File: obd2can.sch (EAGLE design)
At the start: 18 parts, among them Q1 16MHz, SW3 6X3.5_TACT, U2 SN65HVD235DR, U3 STM32F030XTSSOP20, U4 MCP1700, X1 RJ45_RIGHT_ANGLEMOLEX_95001-2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

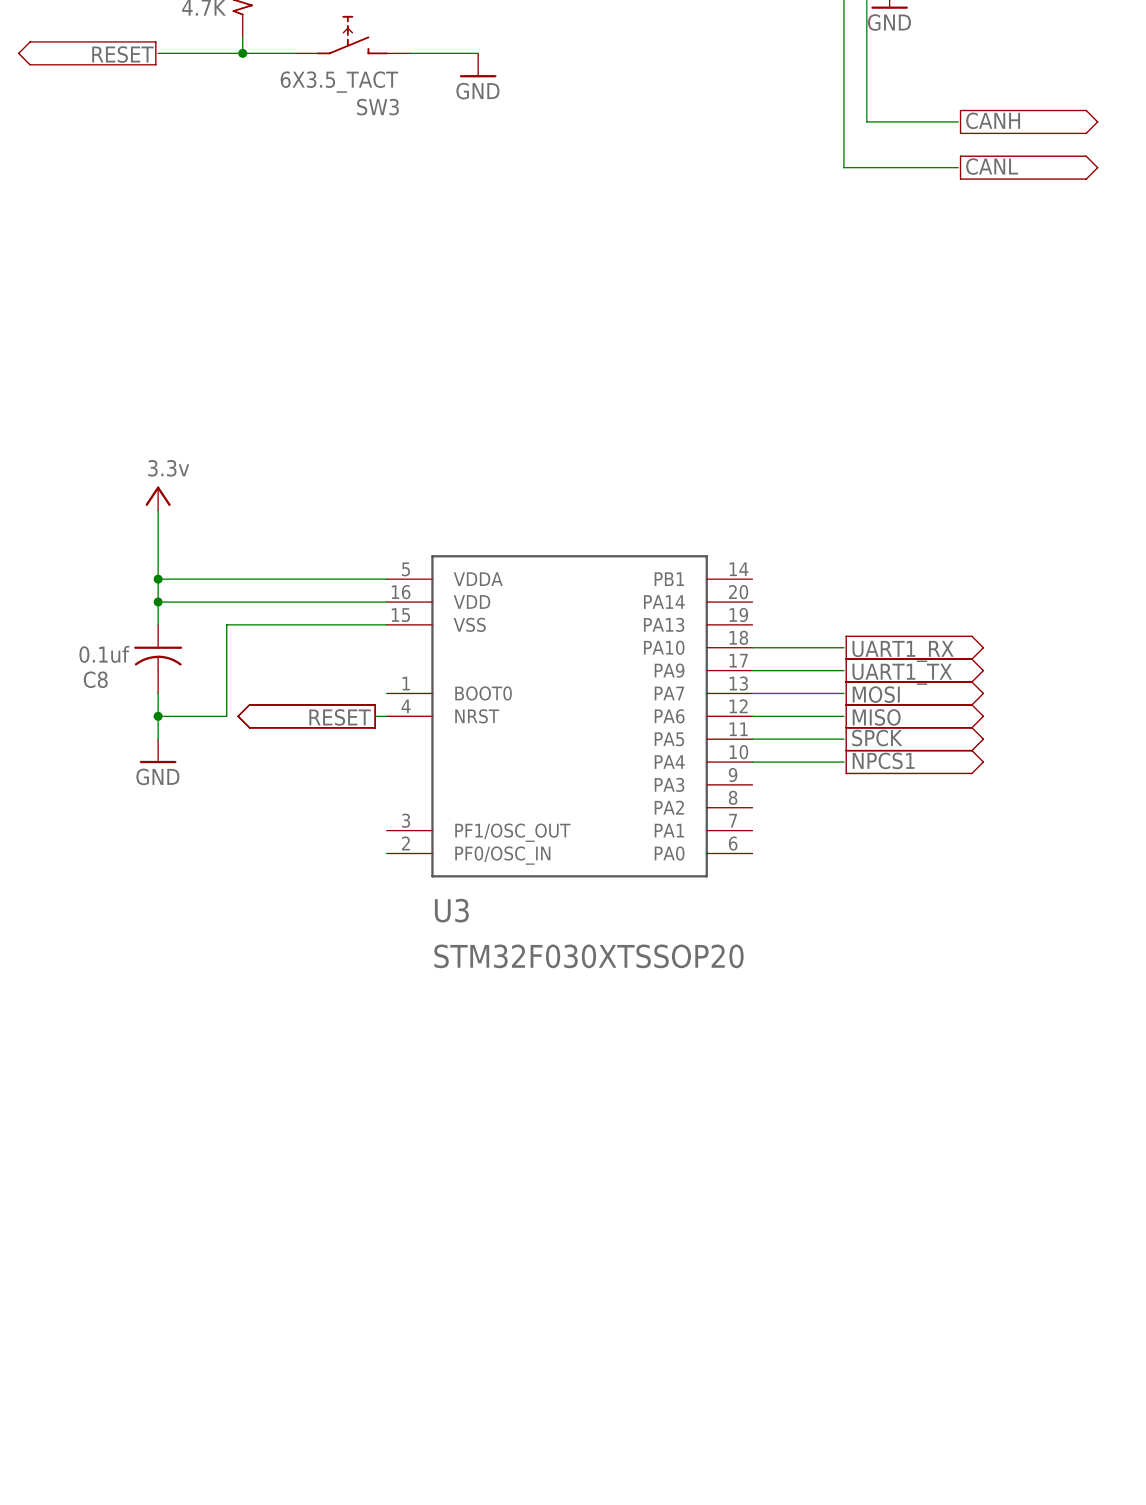
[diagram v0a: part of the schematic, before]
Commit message: added swdebug and boot button
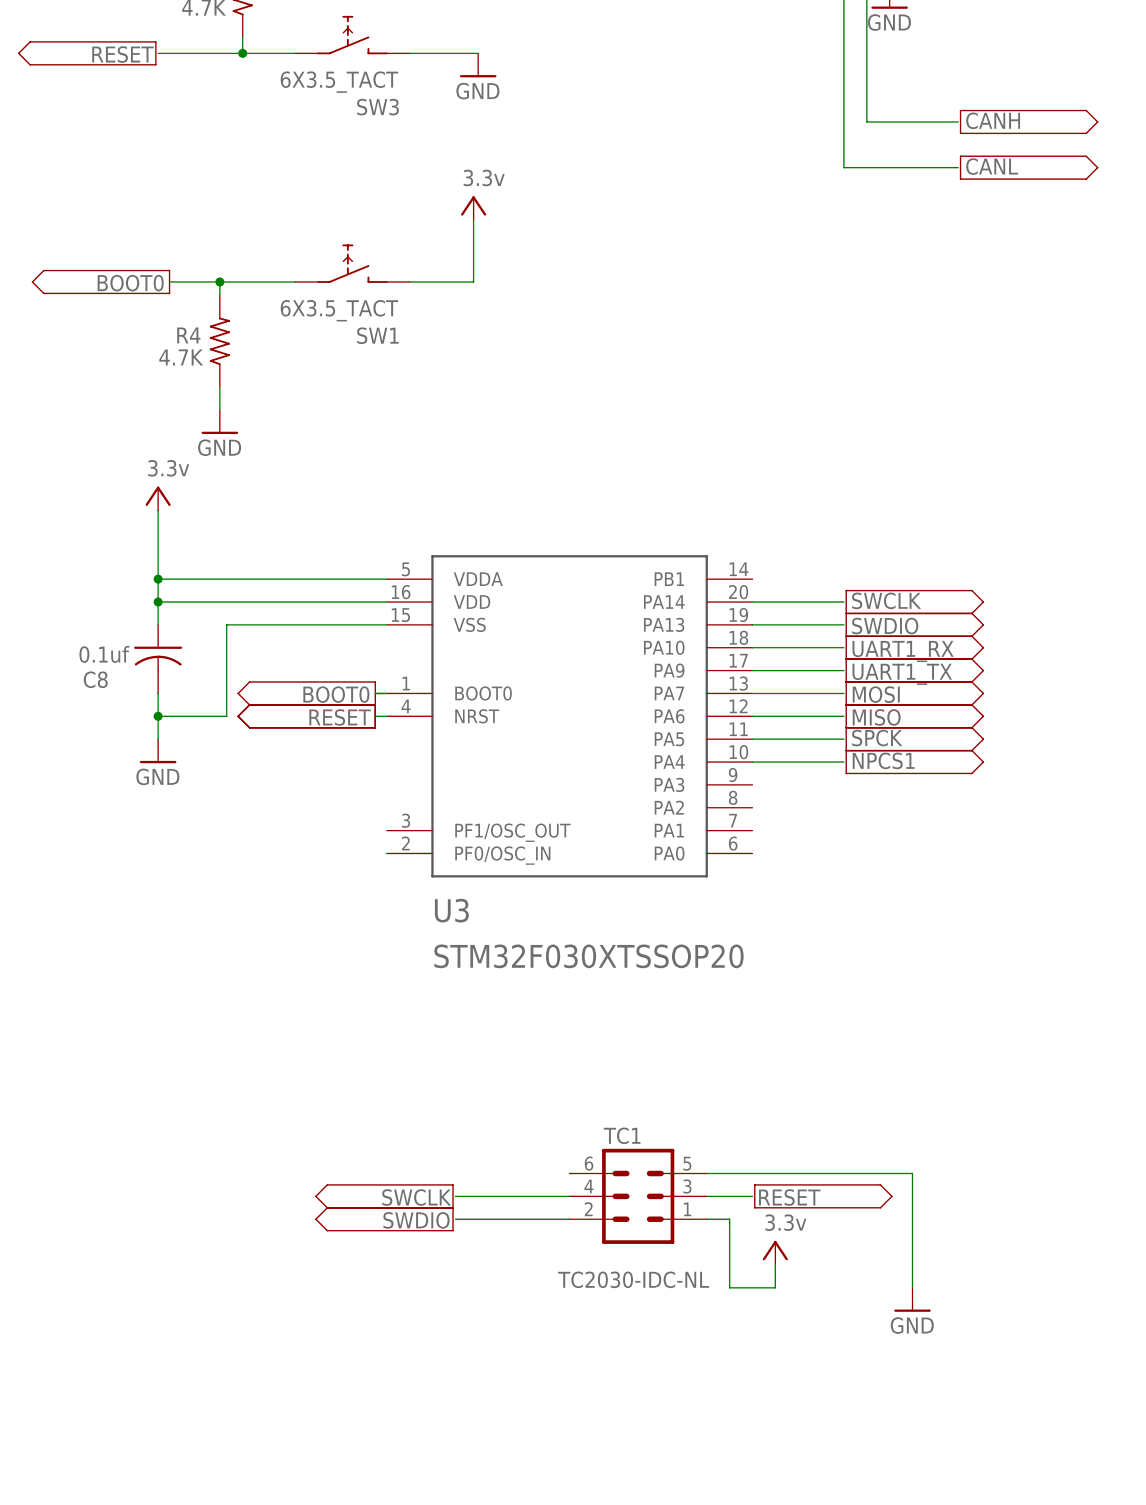
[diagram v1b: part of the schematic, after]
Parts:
- added R4: 4.7K, rcl:R-US_R0603
- added SW1: 6X3.5_TACT, tactile_switch:6X3.5_TACT
- added TC1: TC2030-IDC-NL, TagConnect:TC2030-IDC-NL
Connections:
- new net BOOT0: R4.2, SW1.1, U3.BOOT0
- new net SWCLK: TC1.4, U3.PA14
- new net SWDIO: TC1.2, U3.PA13
- net GND: now also R4.1, TC1.5
- net RESET: now also TC1.3
- net V+: now also SW1.2, TC1.1
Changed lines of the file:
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@@
 <part name="R3" library="rcl" deviceset="R-US_" device="R0603" value="4.7K"/>
 <part name="P+8" library="supply2" deviceset="V+" device="" value="3.3v"/>
+<part name="TC1" library="TagConnect" deviceset="TC2030-IDC" device="-NL"/>
+<part name="GND6" library="supply1" deviceset="GND" device=""/>
+<part name="P+9" library="supply2" deviceset="V+" device="" value="3.3v"/>
+<part name="AD14" library="supply2" deviceset="V--&gt;" device="" value=""/>
+<part name="AD15" library="supply2" deviceset="V--&gt;" device="" value=""/>
+<part name="AD16" library="supply2" deviceset="V--&gt;" device="" value=""/>
+<part name="AD17" library="supply2" deviceset="V--&gt;" device="" value=""/>
+<part name="AD18" library="supply2" deviceset="V--&gt;" device="" value=""/>
+<part name="AD19" library="supply2" deviceset="V--&gt;" device="" value=""/>
+<part name="SW1" library="tactile_switch" deviceset="6X3.5_TACT" device=""/>
+<part name="R4" library="rcl" deviceset="R-US_" device="R0603" value="4.7K"/>
+<part name="GND9" library="supply1" deviceset="GND" device=""/>
+<part name="P+10" library="supply2" deviceset="V+" device="" value="3.3v"/>
+<part name="AD20" library="supply2" deviceset="V--&gt;" device="" value=""/>
 </parts>
 <sheets>
@@
 </instance>
 <instance part="P+8" gate="1" x="-71.882" y="38.862"/>
+<instance part="TC1" gate="A" x="-27.94" y="-106.68" smashed="yes">
+<attribute name="VALUE" x="-36.83" y="-116.84" size="1.778" layer="96"/>
+<attribute name="NAME" x="-31.75" y="-100.838" size="1.778" layer="95"/>
+</instance>
+<instance part="GND6" gate="1" x="2.54" y="-119.38"/>
+<instance part="P+9" gate="1" x="-12.7" y="-111.76"/>
+<instance part="AD14" gate="G$1" x="-48.514" y="-109.22" smashed="yes" rot="R180">
+<attribute name="VALUE" x="-49.784" y="-108.458" size="1.778" layer="96" rot="R180"/>
+</instance>
+<instance part="AD15" gate="G$1" x="-48.514" y="-106.68" smashed="yes" rot="R180">
+<attribute name="VALUE" x="-49.784" y="-105.918" size="1.778" layer="96" rot="R180"/>
+</instance>
+<instance part="AD16" gate="G$1" x="-14.986" y="-106.68" smashed="yes">
+<attribute name="VALUE" x="-13.716" y="-107.442" size="1.778" layer="96"/>
+</instance>
+<instance part="AD17" gate="G$1" x="-4.826" y="-43.18" smashed="yes">
+<attribute name="VALUE" x="-3.556" y="-43.942" size="1.778" layer="96"/>
+</instance>
+<instance part="AD18" gate="G$1" x="-4.826" y="-40.64" smashed="yes">
+<attribute name="VALUE" x="-3.556" y="-41.402" size="1.778" layer="96"/>
+</instance>
+<instance part="AD19" gate="G$1" x="-57.15" y="-50.8" smashed="yes" rot="R180">
+<attribute name="VALUE" x="-58.42" y="-50.038" size="1.778" layer="96" rot="R180"/>
+</instance>
+<instance part="SW1" gate="G$1" x="-60.96" y="-5.08" smashed="yes">
+<attribute name="NAME" x="-54.356" y="-10.16" size="1.778" layer="95" rot="R180"/>
+<attribute name="VALUE" x="-54.61" y="-7.112" size="1.778" layer="96" rot="R180"/>
+</instance>
+<instance part="R4" gate="G$1" x="-74.422" y="-11.684" smashed="yes" rot="R90">
+<attribute name="NAME" x="-76.454" y="-10.1346" size="1.778" layer="95" rot="R180"/>
+<attribute name="VALUE" x="-76.327" y="-12.573" size="1.778" layer="96" rot="R180"/>
+</instance>
+<instance part="GND9" gate="1" x="-74.422" y="-21.844"/>
+<instance part="P+10" gate="1" x="-46.228" y="4.318"/>
+<instance part="AD20" gate="G$1" x="-80.01" y="-5.08" smashed="yes" rot="R180">
+<attribute name="VALUE" x="-81.28" y="-4.318" size="1.778" layer="96" rot="R180"/>
+</instance>
 </instances>
 <busses>
@@
 <pinref part="SW3" gate="G$1" pin="2"/>
 <pinref part="GND46" gate="1" pin="GND"/>
+</segment>
+<segment>
+<pinref part="GND6" gate="1" pin="GND"/>
+<wire x1="2.54" y1="-104.14" x2="2.54" y2="-116.84" width="0.1524" layer="91"/>
+<pinref part="TC1" gate="A" pin="5"/>
+<wire x1="2.54" y1="-104.14" x2="-20.32" y2="-104.14" width="0.1524" layer="91"/>
+</segment>
+<segment>
+<pinref part="R4" gate="G$1" pin="1"/>
+<pinref part="GND9" gate="1" pin="GND"/>
+<wire x1="-74.422" y1="-19.304" x2="-74.422" y2="-16.764" width="0.1524" layer="91"/>
 </segment>
 </net>
@@
 <wire x1="-71.882" y1="36.322" x2="-71.882" y2="32.258" width="0.1524" layer="91"/>
 </segment>
+<segment>
+<pinref part="TC1" gate="A" pin="1"/>
+<wire x1="-20.32" y1="-109.22" x2="-17.78" y2="-109.22" width="0.1524" layer="91"/>
+<wire x1="-17.78" y1="-109.22" x2="-17.78" y2="-116.84" width="0.1524" layer="91"/>
+<pinref part="P+9" gate="1" pin="V+"/>
+<wire x1="-17.78" y1="-116.84" x2="-12.7" y2="-116.84" width="0.1524" layer="91"/>
+<wire x1="-12.7" y1="-116.84" x2="-12.7" y2="-114.3" width="0.1524" layer="91"/>
+</segment>
+<segment>
+<pinref part="P+10" gate="1" pin="V+"/>
+<pinref part="SW1" gate="G$1" pin="2"/>
+<wire x1="-46.228" y1="1.778" x2="-46.228" y2="-5.08" width="0.1524" layer="91"/>
+<wire x1="-46.228" y1="-5.08" x2="-53.34" y2="-5.08" width="0.1524" layer="91"/>
+</segment>
 </net>
 <net name="UART1_TX" class="0">
@@
 <label x="-57.658" y="-52.578" size="1.778" layer="95" rot="R180"/>
 </segment>
+<segment>
+<pinref part="TC1" gate="A" pin="3"/>
+<wire x1="-20.32" y1="-106.68" x2="-15.24" y2="-106.68" width="0.1524" layer="91"/>
+<label x="-14.732" y="-107.696" size="1.778" layer="95"/>
+</segment>
 </net>
+<net name="SWDIO" class="0">
+<segment>
+<pinref part="TC1" gate="A" pin="2"/>
+<wire x1="-35.56" y1="-109.22" x2="-48.26" y2="-109.22" width="0.1524" layer="91"/>
+<label x="-48.768" y="-108.458" size="1.778" layer="95" rot="R180"/>
+</segment>
+<segment>
+<pinref part="U3" gate="G$1" pin="PA13"/>
+<wire x1="-15.24" y1="-43.18" x2="-5.08" y2="-43.18" width="0.1524" layer="91"/>
+<label x="-4.318" y="-44.196" size="1.778" layer="95"/>
+</segment>
+</net>
+<net name="SWCLK" class="0">
+<segment>
+<pinref part="TC1" gate="A" pin="4"/>
+<wire x1="-35.56" y1="-106.68" x2="-48.26" y2="-106.68" width="0.1524" layer="91"/>
+<label x="-48.768" y="-105.918" size="1.778" layer="95" rot="R180"/>
+</segment>
+<segment>
+<pinref part="U3" gate="G$1" pin="PA14"/>
+<wire x1="-15.24" y1="-40.64" x2="-5.08" y2="-40.64" width="0.1524" layer="91"/>
+<label x="-4.318" y="-41.402" size="1.778" layer="95"/>
+</segment>
+</net>
+<net name="BOOT0" class="0">
+<segment>
+<pinref part="U3" gate="G$1" pin="BOOT0"/>
+<wire x1="-55.88" y1="-50.8" x2="-57.15" y2="-50.8" width="0.1524" layer="91"/>
+<wire x1="-55.88" y1="-50.8" x2="-57.15" y2="-50.8" width="0.1524" layer="91"/>
+<label x="-57.658" y="-50.038" size="1.778" layer="95" rot="R180"/>
+</segment>
+<segment>
+<pinref part="SW1" gate="G$1" pin="1"/>
+<wire x1="-66.04" y1="-5.08" x2="-74.422" y2="-5.08" width="0.1524" layer="91"/>
+<pinref part="R4" gate="G$1" pin="2"/>
+<wire x1="-74.422" y1="-5.08" x2="-80.01" y2="-5.08" width="0.1524" layer="91"/>
+<wire x1="-74.422" y1="-6.604" x2="-74.422" y2="-5.08" width="0.1524" layer="91"/>
+<junction x="-74.422" y="-5.08"/>
+<label x="-80.518" y="-4.318" size="1.778" layer="95" rot="R180"/>
+</segment>
+</net>

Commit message: minor label updates
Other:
- note added: "Copyright 2014 Autosport Labs"
- note added: "OBD to CAN bus bridge"
- note added: "OBD2CAN"
- note removed: "CAN bus expansion for RaceCapture/Pro"
- note removed: "CANx"
- note removed: "Copyright 2012-2013 Autosport Labs"
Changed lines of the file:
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@@
 <setting verticaltext="up"/>
 </settings>
-<grid distance="0.01" unitdist="inch" unit="inch" style="lines" multiple="1" display="no" altdistance="0.01" altunitdist="inch" altunit="inch"/>
+<grid distance="0.1" unitdist="inch" unit="inch" style="lines" multiple="1" display="no" altdistance="0.01" altunitdist="inch" altunit="inch"/>
 <layers>
 <layer number="1" name="Top" color="4" fill="1" visible="no" active="no"/>
@@
 <sheet>
 <plain>
-<text x="353.06" y="175.26" size="6.4516" layer="97" rot="R180">Copyright 2012-2013 Autosport Labs</text>
-<text x="353.06" y="195.58" size="6.4516" layer="97" rot="R180">CANx</text>
+<text x="353.06" y="175.26" size="6.4516" layer="97" rot="R180">Copyright 2014 Autosport Labs</text>
+<text x="353.06" y="195.58" size="6.4516" layer="97" rot="R180">OBD2CAN</text>
 <text x="265.43" y="206.883" size="6.4516" layer="97" font="vector">autosportlabs.net</text>
 <text x="359.918" y="-179.832" size="5.08" layer="97">A</text>
-<text x="353.06" y="185.42" size="6.4516" layer="97" rot="R180">CAN bus expansion for RaceCapture/Pro</text>
+<text x="353.06" y="185.42" size="6.4516" layer="97" rot="R180">OBD to CAN bus bridge</text>
 <rectangle x1="284.6705" y1="215.9635" x2="355.5365" y2="216.0905" layer="97"/>
 <rectangle x1="284.6705" y1="216.0905" x2="355.5365" y2="216.2175" layer="97"/>

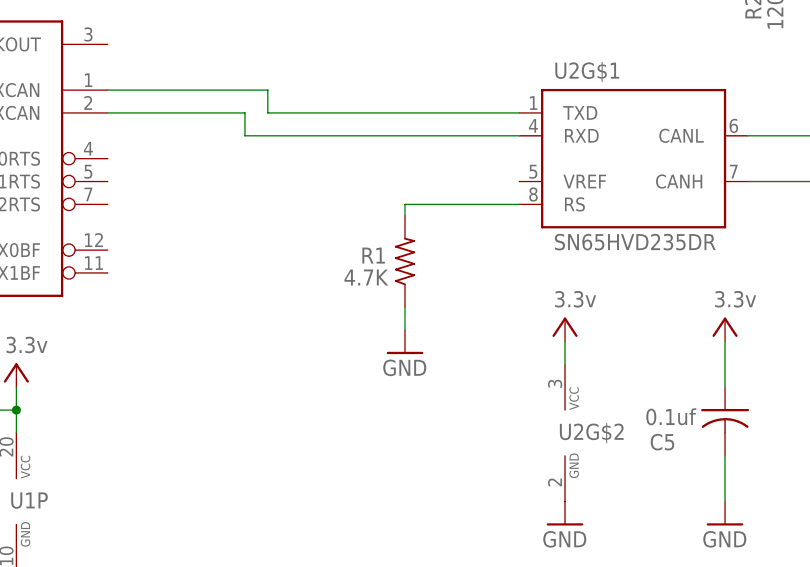
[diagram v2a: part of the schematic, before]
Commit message: grounded vref pin on can transceiver
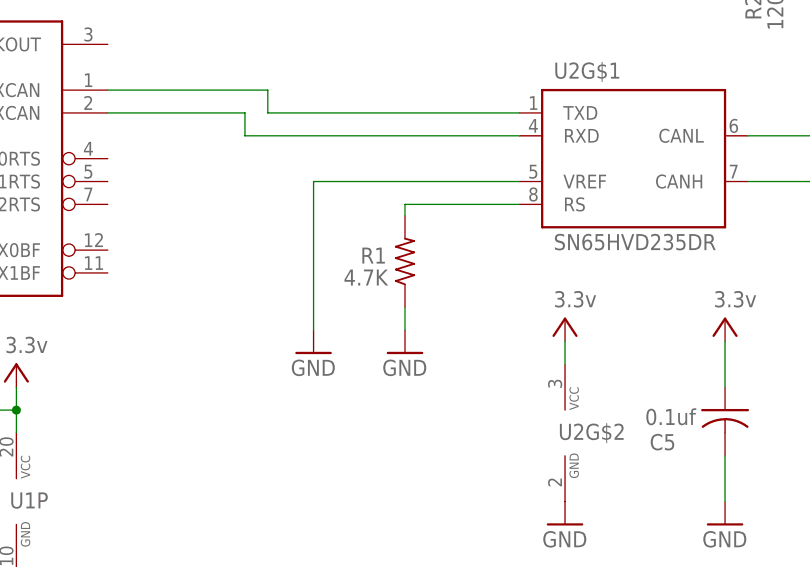
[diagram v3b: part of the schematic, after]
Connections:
- net GND: now also U2G$1.VREF
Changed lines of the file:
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@@
 <setting verticaltext="up"/>
 </settings>
-<grid distance="0.1" unitdist="inch" unit="inch" style="lines" multiple="1" display="no" altdistance="0.01" altunitdist="inch" altunit="inch"/>
+<grid distance="0.01" unitdist="inch" unit="inch" style="lines" multiple="1" display="no" altdistance="0.01" altunitdist="inch" altunit="inch"/>
 <layers>
 <layer number="1" name="Top" color="4" fill="1" visible="no" active="no"/>
@@
 <part name="P+10" library="supply2" deviceset="V+" device="" value="3.3v"/>
 <part name="AD20" library="supply2" deviceset="V--&gt;" device="" value=""/>
+<part name="GND11" library="supply1" deviceset="GND" device=""/>
 </parts>
 <sheets>
@@
 <attribute name="VALUE" x="-81.28" y="-4.318" size="1.778" layer="96" rot="R180"/>
 </instance>
+<instance part="GND11" gate="1" x="142.24" y="13.97"/>
 </instances>
 <busses>
@@
 <wire x1="-74.422" y1="-19.304" x2="-74.422" y2="-16.764" width="0.1524" layer="91"/>
 </segment>
+<segment>
+<pinref part="U2" gate="G$1" pin="VREF"/>
+<wire x1="165.1" y1="33.02" x2="142.24" y2="33.02" width="0.1524" layer="91"/>
+<wire x1="142.24" y1="33.02" x2="142.24" y2="16.51" width="0.1524" layer="91"/>
+<pinref part="GND11" gate="1" pin="GND"/>
+</segment>
 </net>

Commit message: OBD2CAN WIP
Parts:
- removed C4: 0.1uF, rcl:C-USC0603K
- removed C6: 10uF, rcl:CPOL-USSMCA
- removed C8: 0.1uf, rcl:C-USC0603K
- removed SW1, SW3: 6X3.5_TACT, tactile_switch:6X3.5_TACT
- removed TC1: TC2030-IDC-NL, TagConnect:TC2030-IDC-NL
- removed U4: MCP1700, mcp1700:MCP1700
- added C10: 1uf, rcl:C-USC0603K
- added C11: 0.01uf, rcl:C-USC0603K
- added C12, C15: 4.7uf, rcl:C-USC0603K
- added C14, C9: 0.1uf, rcl:C-USC0603K
- added C25, C28: 22uF, rcl:C-USC1206
- added C27: 10nF, rcl:C-USC0603
- added D1: SCHOTTKY, smt_diodes:SCHOTTKY
- added D2: 400V 1A, smt_diodes:DIODE1
- added D5: (no value), diode:SCHOTTKY-DIODESMC
- added L1: 4.7uH, rcl:L-EUL2012C
- added L2: (no value), wuerth-elektronik:WE-CBF_1812
- added R5: 4.7K, rcl:R-US_R0603
- added SW2: 6X3.5_TACT, tactile_switch:6X3.5_TACT
- added TC2: TC2030-IDC-NL, TagConnect:TC2030-IDC-NL
- added TP2: TPB1,27, testpad:TPB1,27
- added X2: RJ45_RIGHT_ANGLEMOLEX_95001-2881, FCI_RJ12:RJ45_RIGHT_ANGLEMOLEX_95001-2881
- C2, C3: value 22pF -> 33pF; device rcl:C-USC0603K -> SparkFun:CAP0603
- Q1: value 16MHz -> 8MHz; device SparkFun:CRYSTAL5X3 -> SparkFun2:CRYSTAL5X3
- R3: value 4.7K -> 16.2K 1%
- R4: value 4.7K -> 49.9K 1%
- U1: value (none) -> AP3211KTR-G1; device can:MCP2515ST -> diodes_inc:AP3211KTR-G1
- U3: value STM32F030XTSSOP20 -> STM32F072-LQFP48; device stm32f030x:STM32F030XTSSOP20 -> stm32f0:STM32F072-LQFP48
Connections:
- removed net BOOT0: R4.2, SW1.1, U3.BOOT0
- removed net CAN1_RX: U1D.RXCAN, U2G$1.RXD
- removed net CAN1_TX: U1D.TXCAN, U2G$1.TXD
- removed net MISO: U1D.SO, U3.PA6
- removed net MOSI: U1D.SI, U3.PA7
- removed net N$2: C3.1, Q1.1, U1D.OSC2
- removed net NPCS1: U1D.CS, U3.PA4
- removed net SPCK: U1D.SCK, U3.PA5
- removed net UART1_RX: SV1.4, U3.PA10
- removed net UART1_TX: SV1.5, U3.PA9
- new net +12V: L2.2, X1.P8, X2.P8
- new net AGND: U3.VSSA(P8)
- new net ANALOG_1_ADC: U3.PA0/USART4_TX/WKUP1/ADC_IN0
- new net CAN_RX: U2G$1.RXD, U3.PA11/USB_DM/CAN_RX
- new net CAN_TX: U2G$1.TXD, U3.PA12/USB_DP/CAN_TX
- new net N$3: TP2.TP, U3.PB0/ADC_IN8/TIM3_CH3
- new net N$40: C2.2, Q1.2, U3.PF1/OSC_OUT
- new net N$42: C3.2, Q1.1, U3.PF0/OSC_IN
- new net N$5: C27.2, U1.BS
- new net N$50: D2.A, L2.1
- new net N$6: C27.1, D1.C, L1.1, U1.SW
- new net SAFE12V: C25.1, D2.C, D5.C, U1.EN, U1.IN
- new net U3: R4.1, R5.2, TC2.1
- new net USART1_RX: SV1.4, U3.PA10/USART1_RX/TIM1_CH3
- new net USART1_TX: SV1.5, U3.PA9/USART1_TX/TIM1_CH2
- new net USART2_RX: U3.PA3/ADC_IN3/COMP2_INP/USART2_RX
- new net USART2_TX: U3.PA2/ADC_IN2/WKUP4USART2_TX
- net +5V: no longer C6.+, U4.VIN
- net GND: now also C10.2, C11.2, C12.2, C14.2, C15.2, C2.1, C25.2, C28.2, C3.1, C9.2, D1.A, D5.A, R3.2, SW2.2, TC2.5, U1.GND, U3.BOOT0(P44), U3.VSS_1(P23), U3.VSS_2(P35), U3.VSS_3(P47), X2.P1; no longer C2.2, C3.2, C4.2, C6.-, C8.2, R4.1, SW3.2, TC1.5, U1P.GND, U3.VSS, U4.GND
- net N$1: now also R3.1, R4.2, U1.FB; no longer C2.1, Q1.2, U1D.OSC1
- net RESET: now also R5.1, SW2.1, TC2.3, U3.NRST(P7); no longer R3.1, SW3.1, TC1.3, U1D.RESET, U3.NRST
- net SWCLK: now also TC2.4, U3.PA14/USART2_TX/SWCLK; no longer TC1.4, U3.PA14
- net SWDIO: now also TC2.2, U3.PA13/SWDIO; no longer TC1.2, U3.PA13
- net V+: now also C10.1, C11.1, C12.1, C14.1, C15.1, C28.1, C9.1, L1.2, U3.VBATT(P1), U3.VDDA(P9), U3.VDDIO2(P36), U3.VDD_1(P24), U3.VDD_2(P48); no longer C4.1, C8.1, R3.2, SW1.2, TC1.1, U1P.VCC, U3.VDD, U3.VDDA, U4.VOUT
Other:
- note added: "Copyright 2014 - 2015 Autosport Labs"
- note removed: "Copyright 2014 Autosport Labs"
